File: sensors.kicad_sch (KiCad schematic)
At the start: 0 parts

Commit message: update sensor schematic
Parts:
- added MK1: CMC-5042PF-AC, CMC-5042PF-AC:CUI_CMC-5042PF-AC, symbol CMC-5042PF-AC:CMC-5042PF-AC
- added Q1: TEMT6000X01, TEMT6000X01:TRANS_TEMT6000X01, symbol TEMT6000X01:TEMT6000X01
- added U6: BME280, Package_LGA:Bosch_LGA-8_2.5x2.5mm_P0.65mm_ClockwisePinNumbering, symbol Sensor:BME280
- added U7: MAX4466EXK, MAX4466EXK:SOT65P210X110-5N, symbol MAX4466EXK:MAX4466EXK

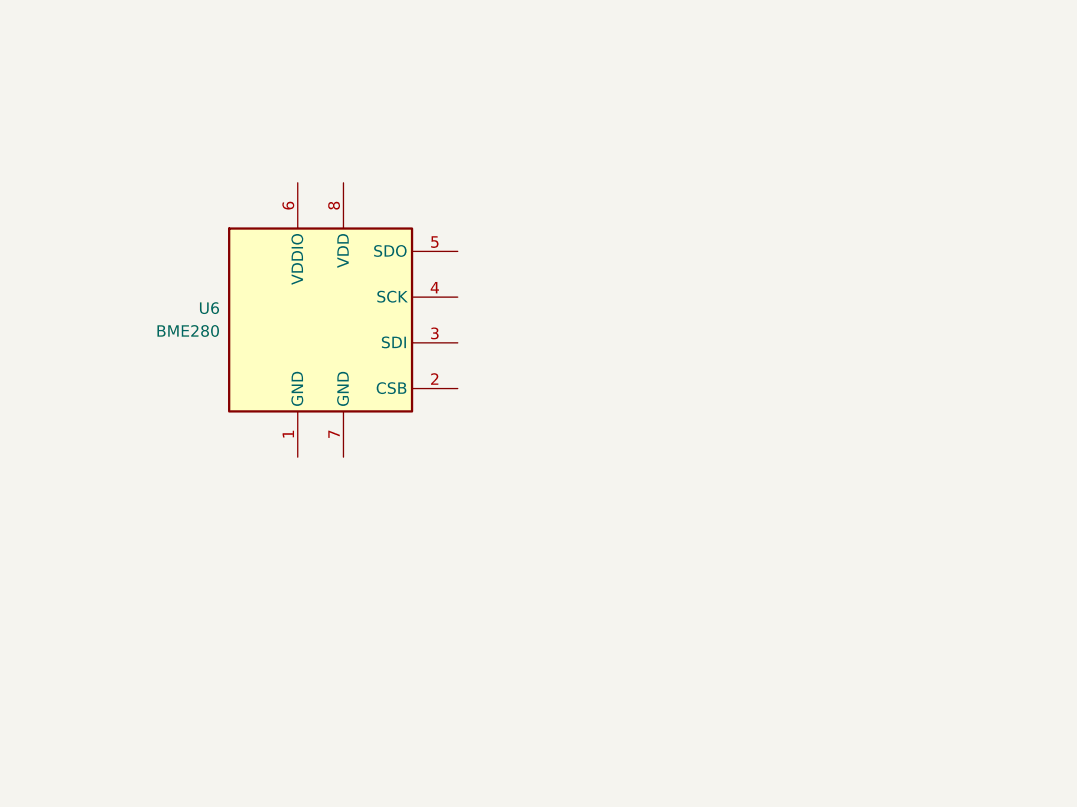
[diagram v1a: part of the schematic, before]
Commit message: implementationo of the BME280 sensor
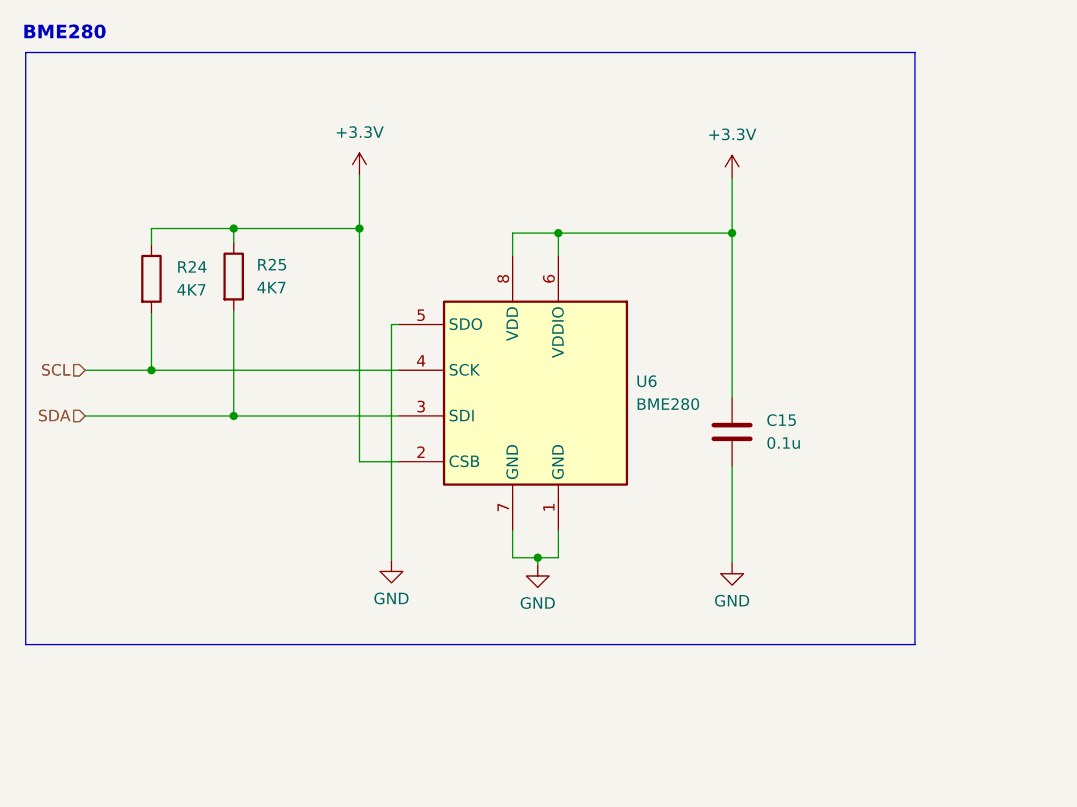
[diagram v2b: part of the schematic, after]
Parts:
- added C15: 0.1u, symbol Device:C
- added R24, R25: 4K7, symbol Device:R
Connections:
- net GND: now reaches U6.1 (GND)
- net GND: now also U6.5 (SDO), U6.7 (GND), C15.2
- net +3.3V: now reaches U6.2 (CSB)
- net +3.3V: now also U6.6 (VDDIO), U6.8 (VDD), C15.1, R24.1, R25.1
- net SDA: now reaches U6.3 (SDI)
- net SDA: now also R25.2
- net SCL: now reaches U6.4 (SCK)
- net SCL: now also R24.2
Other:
- note added: "BME280"
- moved on the sheet: U6

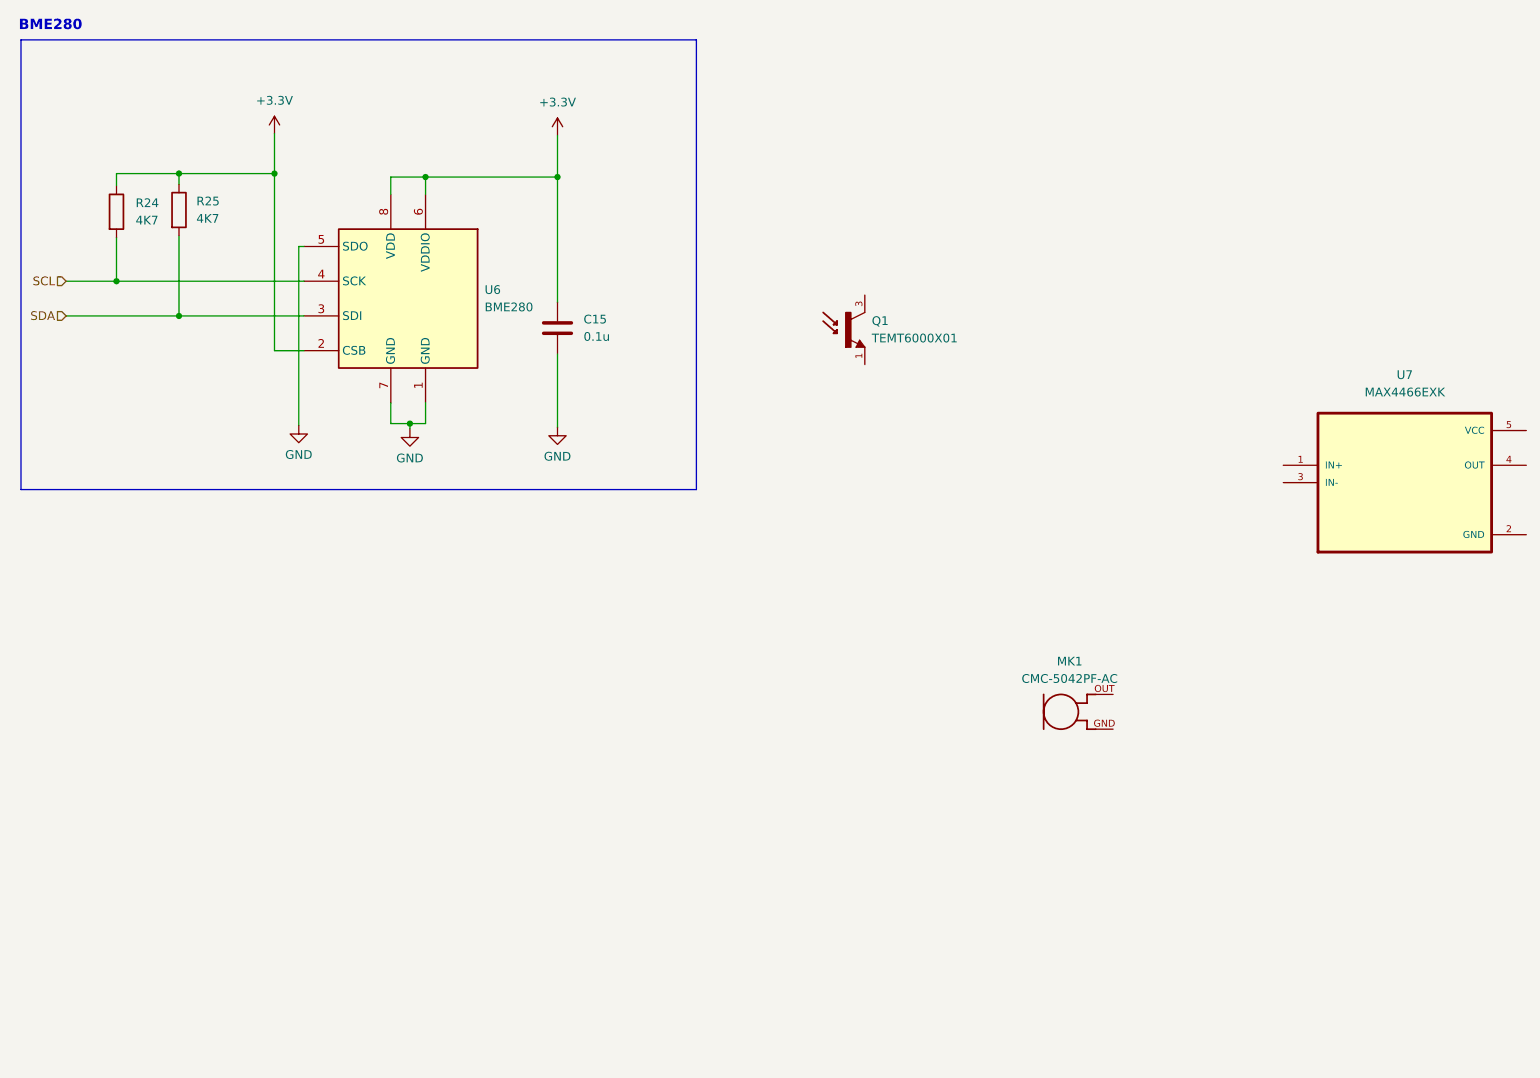
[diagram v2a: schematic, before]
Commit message: connecting hierarchial Pins
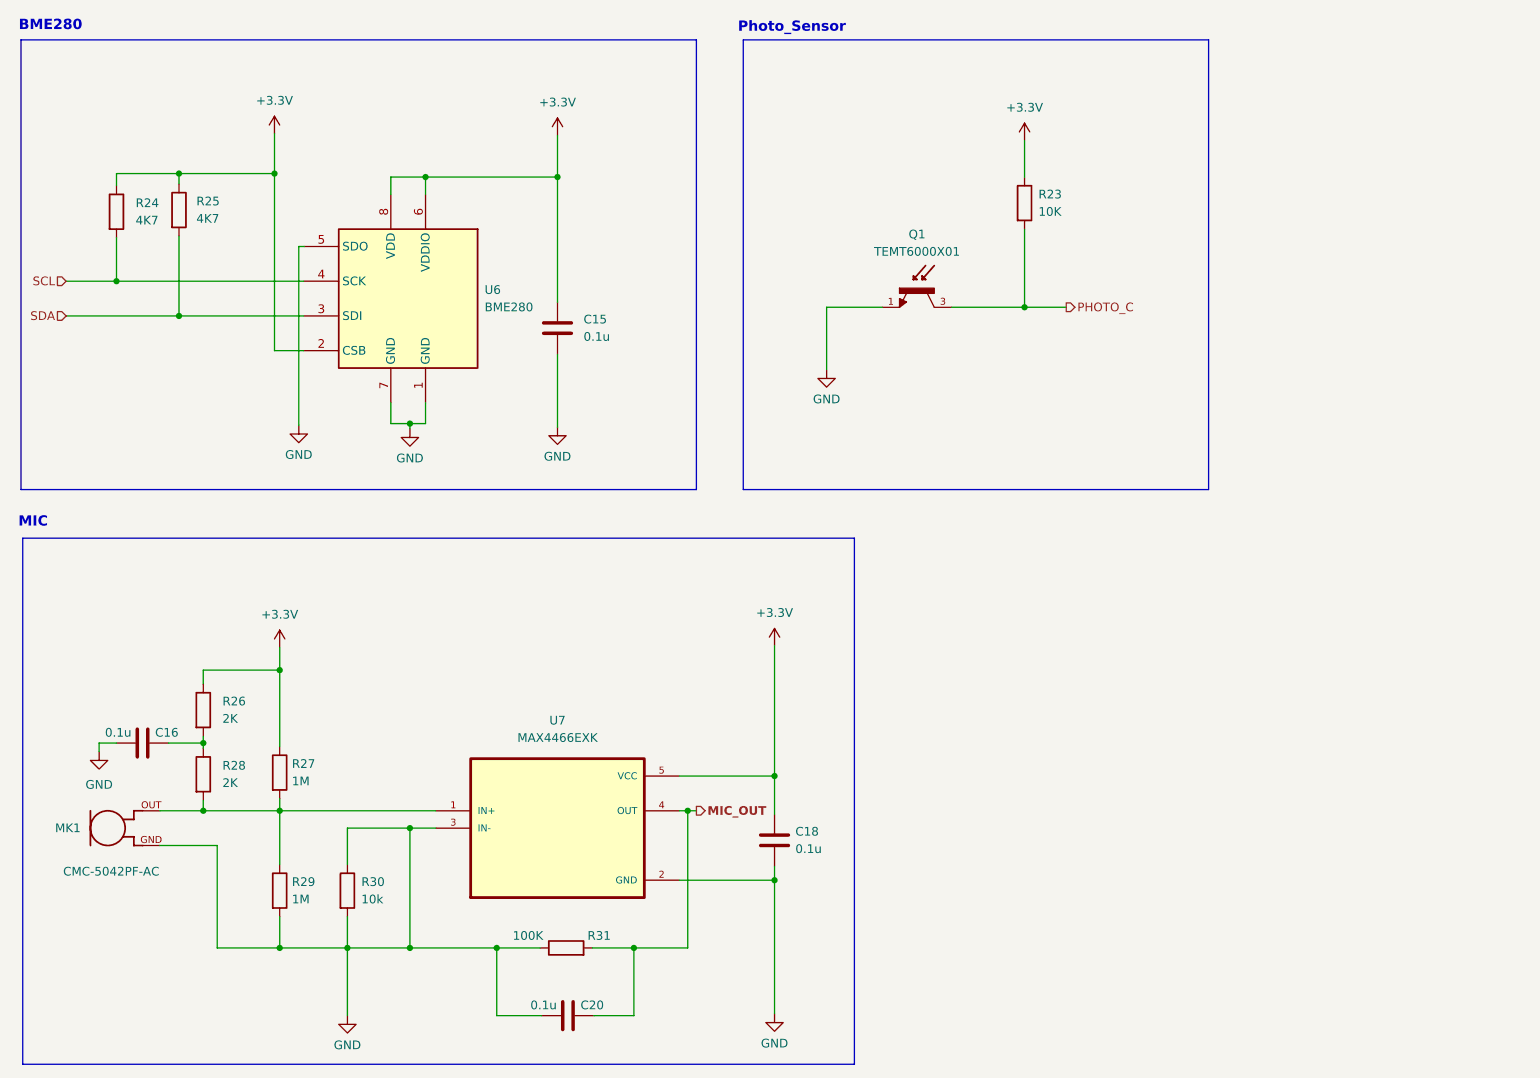
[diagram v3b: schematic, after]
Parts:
- added C16, C18, C20: 0.1u, symbol Device:C
- added R23: 10K, symbol Device:R
- added R26, R28: 2K, symbol Device:R
- added R27, R29: 1M, symbol Device:R
- added R30: 10k, symbol Device:R
- added R31: 100K, symbol Device:R
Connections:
- net +3.3V: now also U7.5 (VCC), C18.1, R23.1, R26.1, R27.1
- net GND: now also MK1.GND, Q1.1, U7.2 (GND), U7.3 (IN-), C16.1, C18.2, C20.1, R29.2, R30.1, R30.2, R31.1
- net PHOTO_C: now reaches Q1.3
- net PHOTO_C: now also R23.2
- net at U7.1 (IN+): now also MK1.OUT, R27.2, R28.2, R29.1
- net MIC_OUT: now reaches U7.4 (OUT)
- net MIC_OUT: now also C20.2, R31.2
- new net: C16.2, R26.2, R28.1
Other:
- note added: "MIC"
- note added: "Photo_Sensor"
- moved on the sheet: MK1, Q1, U7

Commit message: run ERC check for the schematic
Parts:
- C15, C16, C18, C20: footprint (none) -> Capacitor_SMD:C_0805_2012Metric
- R23, R24, R25, R26, R27, R28, R29, R30, R31: footprint (none) -> Resistor_SMD:R_0805_2012Metric
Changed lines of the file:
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@@
 			)
 		)
-		(property "Footprint" ""
+		(property "Footprint" "Resistor_SMD:R_0805_2012Metric"
 			(at 50.038 124.206 90)
 			(effects
@@
 			)
 		)
-		(property "Footprint" ""
+		(property "Footprint" "Resistor_SMD:R_0805_2012Metric"
 			(at 35.306 41.91 90)
 			(effects
@@
 			)
 		)
-		(property "Footprint" ""
+		(property "Footprint" "Capacitor_SMD:C_0805_2012Metric"
 			(at 125.1712 137.922 0)
 			(effects
@@
 			)
 		)
-		(property "Footprint" ""
+		(property "Footprint" "Resistor_SMD:R_0805_2012Metric"
 			(at 26.162 42.164 90)
 			(effects
@@
 			)
 		)
-		(property "Footprint" ""
+		(property "Footprint" "Resistor_SMD:R_0805_2012Metric"
 			(at 59.944 141.478 90)
 			(effects
@@
 			)
 		)
-		(property "Footprint" ""
+		(property "Footprint" "Capacitor_SMD:C_0805_2012Metric"
 			(at 93.4212 62.992 0)
 			(effects
@@
 			)
 		)
-		(property "Footprint" ""
+		(property "Footprint" "Resistor_SMD:R_0805_2012Metric"
 			(at 93.726 151.638 90)
 			(effects
@@
 			)
 		)
-		(property "Footprint" ""
+		(property "Footprint" "Resistor_SMD:R_0805_2012Metric"
 			(at 50.038 141.478 90)
 			(effects
@@
 			)
 		)
-		(property "Footprint" ""
+		(property "Footprint" "Capacitor_SMD:C_0805_2012Metric"
 			(at 35.56 118.9228 0)
 			(effects
@@
 			)
 		)
-		(property "Footprint" ""
+		(property "Footprint" "Resistor_SMD:R_0805_2012Metric"
 			(at 38.862 124.46 90)
 			(effects
@@
 			)
 		)
-		(property "Footprint" ""
+		(property "Footprint" "Resistor_SMD:R_0805_2012Metric"
 			(at 38.862 115.062 90)
 			(effects
@@
 			)
 		)
-		(property "Footprint" ""
+		(property "Footprint" "Capacitor_SMD:C_0805_2012Metric"
 			(at 97.79 158.8008 0)
 			(effects
@@
 			)
 		)
-		(property "Footprint" ""
+		(property "Footprint" "Resistor_SMD:R_0805_2012Metric"
 			(at 159.004 40.894 90)
 			(effects

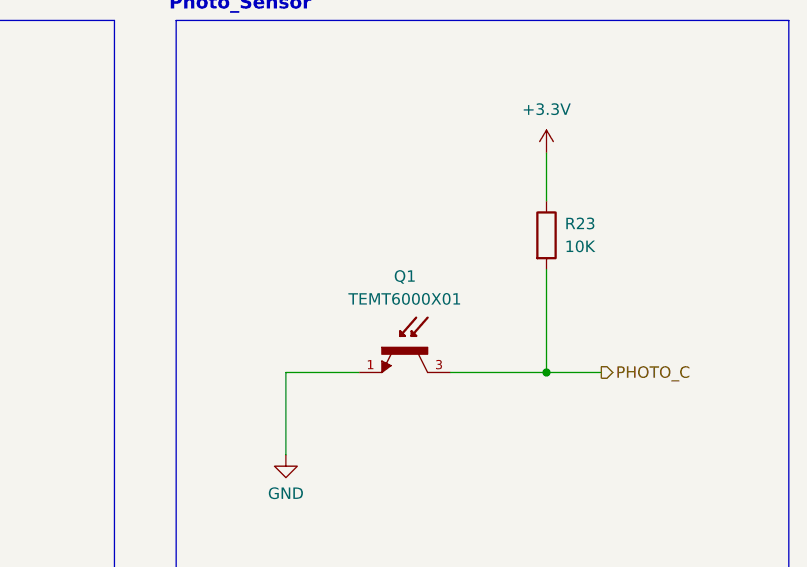
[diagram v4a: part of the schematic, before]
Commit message: assigning footprint, pcb setup and configurations
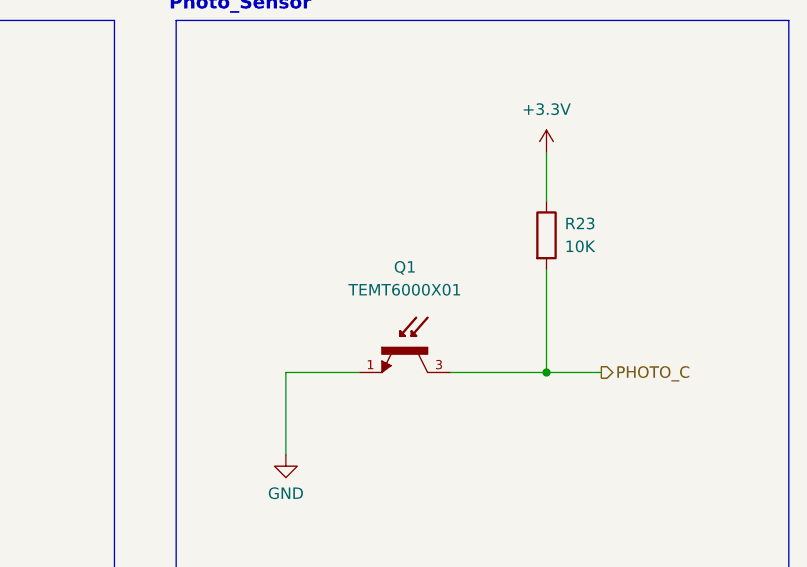
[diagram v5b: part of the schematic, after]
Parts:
- MK1: footprint CMC-5042PF-AC:CUI_CMC-5042PF-AC -> FootPrints:CUI_CMC-5042PF-AC
- Q1: footprint TEMT6000X01:TRANS_TEMT6000X01 -> FootPrints:TRANS_TEMT6000X01
- U7: footprint MAX4466EXK:SOT65P210X110-5N -> FootPrints:SOT65P210X110-5N
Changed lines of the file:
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@@
 		(fields_autoplaced yes)
 		(property "Reference" "Q1"
-			(at 145.0594 45.466 90)
+			(at 145.0594 44.45 90)
 			(effects
 				(font
@@
 		)
 		(property "Value" "TEMT6000X01"
-			(at 145.0594 48.006 90)
-			(effects
-				(font
-					(size 1.27 1.27)
-				)
-			)
-		)
-		(property "Footprint" "TEMT6000X01:TRANS_TEMT6000X01"
+			(at 145.0594 46.99 90)
+			(effects
+				(font
+					(size 1.27 1.27)
+				)
+			)
+		)
+		(property "Footprint" "FootPrints:TRANS_TEMT6000X01"
 			(at 145.034 53.594 0)
 			(effects
@@
 			)
 		)
-		(property "Footprint" "MAX4466EXK:SOT65P210X110-5N"
+		(property "Footprint" "FootPrints:SOT65P210X110-5N"
 			(at 92.456 132.334 0)
 			(effects
@@
 			)
 		)
-		(property "Footprint" "CMC-5042PF-AC:CUI_CMC-5042PF-AC"
+		(property "Footprint" "FootPrints:CUI_CMC-5042PF-AC"
 			(at 26.67 132.334 0)
 			(effects

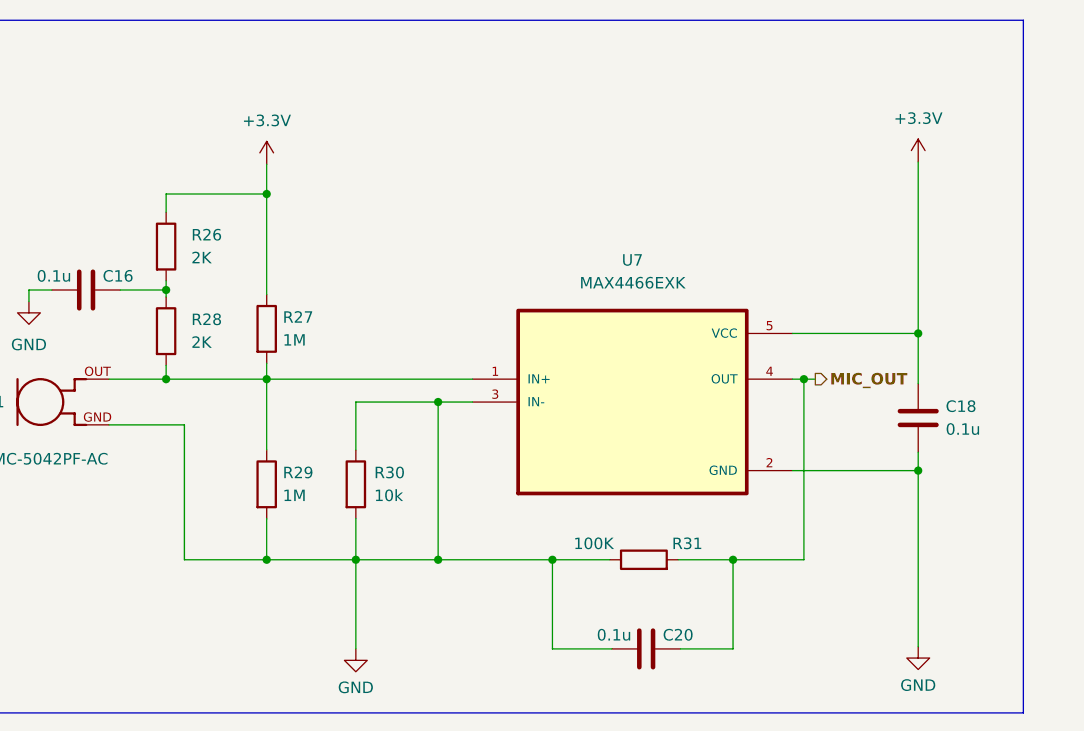
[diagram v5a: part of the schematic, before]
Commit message: update sensor schematic
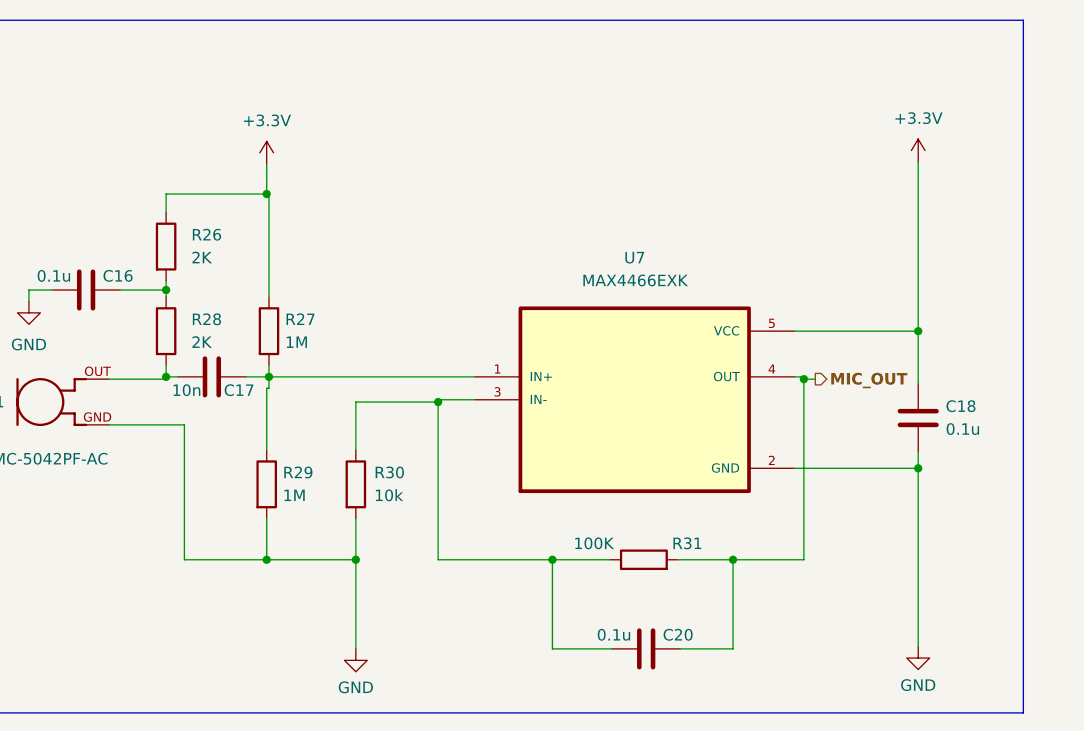
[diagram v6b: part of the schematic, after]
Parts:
- added C17: 10n, Capacitor_SMD:C_0805_2012Metric, symbol Device:C
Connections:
- net GND: no longer C20.1, R30.1, R31.1, U7.3 (IN-)
- net at R27.2, R29.1, U7.1 (IN+): now also C17.2; no longer MK1.OUT, R28.2
- new net: C20.1, R30.1, R31.1, U7.3 (IN-)
- new net: C17.1, MK1.OUT, R28.2
